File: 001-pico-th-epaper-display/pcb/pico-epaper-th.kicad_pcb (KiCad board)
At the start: 2 copper layers, 70 x 70 mm, 16 parts, among them Q1 AO3407, U1 GY-SHT31-D, U2 TPL5110, U3 WS_1_54_epaper_module

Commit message: name change
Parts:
- added C4: 100n, Capacitor_SMD:C_0603_1608Metric_Pad1.08x0.95mm_HandSolder, F.Cu at (149.2, 74.8)
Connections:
- R1 pad 1: Net-(U2-DELAY/M_DRV) -> VCC
- U2 pad 3: Net-(U2-DELAY/M_DRV) -> VCC
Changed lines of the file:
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@@
 		(embedded_fonts no)
 	)
+	(footprint "Capacitor_SMD:C_0603_1608Metric_Pad1.08x0.95mm_HandSolder"
+		(layer "F.Cu")
+		(at 149.175 74.755)
+		(descr "Capacitor SMD 0603 (1608 Metric), square (rectangular) end terminal, IPC-7351 nominal with elongated pad for handsoldering. (Body size source: IPC-SM-782 page 76, https://www.pcb-3d.com/wordpress/wp-content/uploads/ipc-sm-782a_amendment_1_and_2.pdf)")
+		(tags "capacitor handsolder")
+		(property "Reference" "C4"
+			(at 0 -1.43 0)
+			(layer "F.SilkS")
+			(effects
+				(font
+					(size 1 1)
+					(thickness 0.15)
+				)
+			)
+		)
+		(property "Value" "100n"
+			(at 0 1.43 0)
+			(layer "F.Fab")
+			(effects
+				(font
+					(size 1 1)
+					(thickness 0.15)
+				)
+			)
+		)
+		(property "Datasheet" ""
+			(at 0 0 0)
+			(layer "F.Fab")
+			(hide yes)
+			(effects
+				(font
+					(size 1.27 1.27)
+				)
+			)
+		)
+		(property "Description" "Unpolarized capacitor"
+			(at 0 0 0)
+			(layer "F.Fab")
+			(hide yes)
+			(effects
+				(font
+					(size 1.27 1.27)
+				)
+			)
+		)
+		(property "KiLib_Generator" "SMD_2terminal_chip_molded"
+			(at 0 0 0)
+			(layer "F.SilkS")
+			(hide yes)
+			(effects
+				(font
+					(size 1 1)
+					(thickness 0.15)
+				)
+			)
+		)
+		(property ki_fp_filters "C_*")
+		(sheetname "/")
+		(sheetfile "pico-epaper-th.kicad_sch")
+		(units
+			(unit
+				(name "A")
+				(pins "1" "2")
+			)
+		)
+		(attr smd)
+		(duplicate_pad_numbers_are_jumpers no)
+		(fp_line
+			(start -0.146267 -0.51)
+			(end 0.146267 -0.51)
+			(stroke
+				(width 0.12)
+				(type solid)
+			)
+			(layer "F.SilkS")
+		)
+		(fp_line
+			(start -0.146267 0.51)
+			(end 0.146267 0.51)
+			(stroke
+				(width 0.12)
+				(type solid)
+			)
+			(layer "F.SilkS")
+		)
+		(fp_rect
+			(start -1.65 -0.73)
+			(end 1.65 0.73)
+			(stroke
+				(width 0.05)
+				(type solid)
+			)
+			(fill no)
+			(layer "F.CrtYd")
+		)
+		(fp_rect
+			(start -0.8 -0.4)
+			(end 0.8 0.4)
+			(stroke
+				(width 0.1)
+				(type solid)
+			)
+			(fill no)
+			(layer "F.Fab")
+		)
+		(fp_text user "${REFERENCE}"
+			(at 0 0 0)
+			(layer "F.Fab")
+			(effects
+				(font
+					(size 0.4 0.4)
+					(thickness 0.06)
+				)
+			)
+		)
+		(pad "1" smd roundrect
+			(at -0.8625 0)
+			(size 1.075 0.95)
+			(layers "F.Cu" "F.Mask" "F.Paste")
+			(roundrect_rratio 0.25)
+			(net "Net-(A1-VSYS)")
+			(pintype "passive")
+		)
+		(pad "2" smd roundrect
+			(at 0.8625 0)
+			(size 1.075 0.95)
+			(layers "F.Cu" "F.Mask" "F.Paste")
+			(roundrect_rratio 0.25)
+			(net "GND")
+			(pintype "passive")
+		)
+		(embedded_fonts no)
+		(model "${KICAD10_3DMODEL_DIR}/Capacitor_SMD.3dshapes/C_0603_1608Metric.step"
+			(offset
+				(xyz 0 0 0)
+			)
+			(scale
+				(xyz 1 1 1)
+			)
+			(rotate
+				(xyz 0 0 0)
+			)
+		)
+	)
 	(footprint "MountingHole:MountingHole_2.2mm_M2_Pad"
 		(layer "F.Cu")
@@
 			(layers "F.Cu" "F.Mask" "F.Paste")
 			(roundrect_rratio 0.25)
-			(net "Net-(U2-DELAY{slash}M_DRV)")
+			(net "VCC")
 			(pinfunction "DELAY/M_DRV_3")
 			(pintype "input")
@@
 			(layers "F.Cu" "F.Mask" "F.Paste")
 			(roundrect_rratio 0.25)
-			(net "Net-(U2-DELAY{slash}M_DRV)")
+			(net "VCC")
 			(pintype "passive")
 		)
@@
 		(model "${KIPRJMOD}/AABattery Holder.stp"
 			(offset
-				(xyz -48 -60 -10)
+				(xyz -48 -57 -10)
 			)
 			(scale

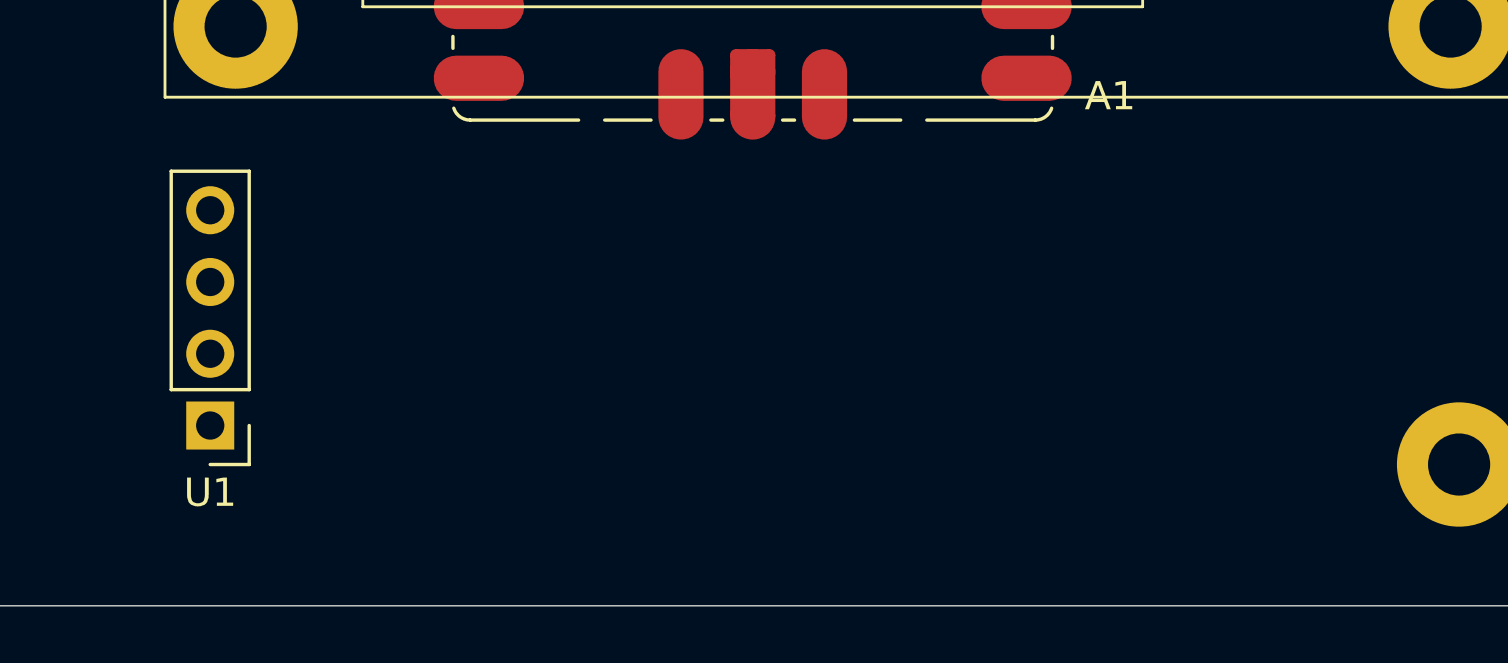
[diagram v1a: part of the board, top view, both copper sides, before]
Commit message: pin changed for sht31
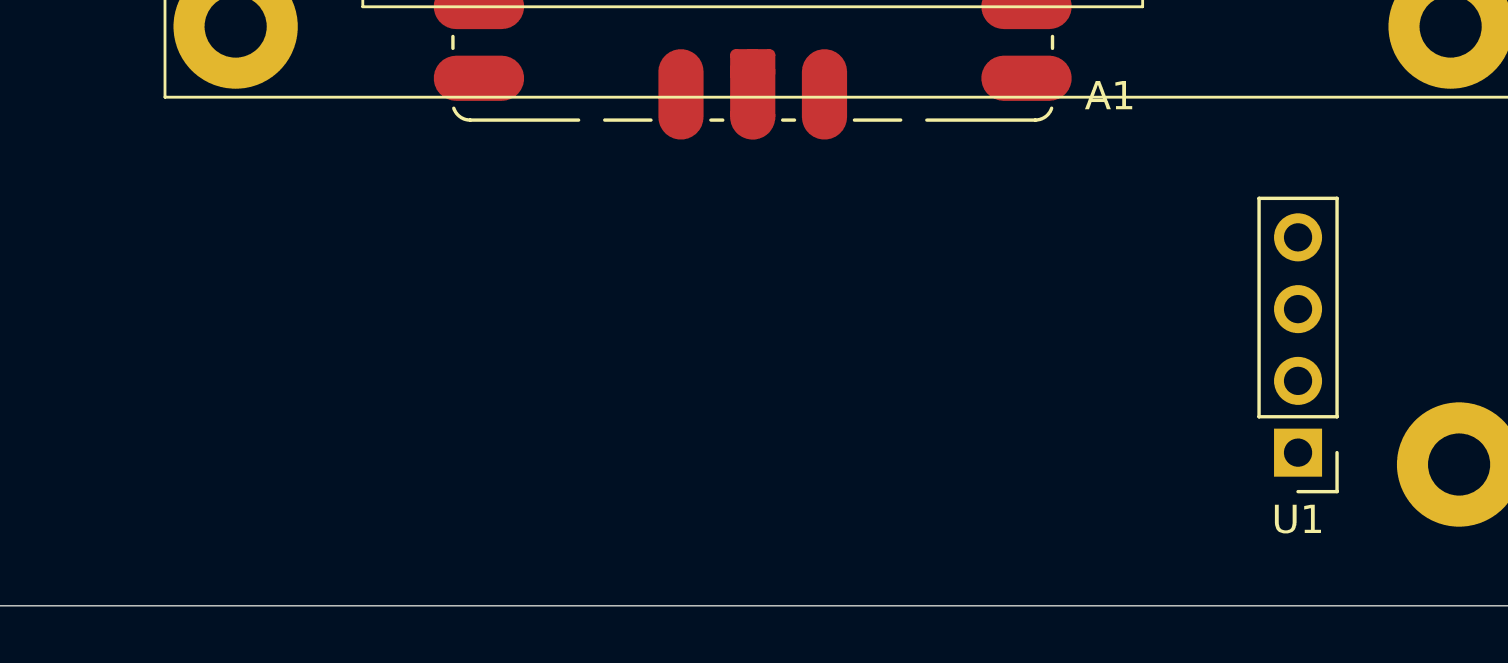
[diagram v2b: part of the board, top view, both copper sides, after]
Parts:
- moved U1 38.5 mm to (154.7, 136.9)
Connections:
- net Net-(A1-3V3) renamed /3V3
- A1 pad 26: unconnected-(A1-GPIO20-Pad26) -> Net-(A1-GPIO20)
- A1 pad 27: unconnected-(A1-GPIO21-Pad27) -> Net-(A1-GPIO21)
- A1 pad 6: Net-(A1-GPIO4) -> unconnected-(A1-GPIO4-Pad6)
- A1 pad 7: Net-(A1-GPIO5) -> unconnected-(A1-GPIO5-Pad7)
- U1 pad 3: Net-(A1-GPIO5) -> Net-(A1-GPIO21)
- U1 pad 4: Net-(A1-GPIO4) -> Net-(A1-GPIO20)
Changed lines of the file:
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@@
 			(layers "*.Cu" "*.Mask")
 			(remove_unused_layers no)
-			(net "Net-(A1-3V3)")
+			(net "/3V3")
 			(pinfunction "VCC_8")
 			(pintype "power_in")
@@
 			(layers "F.Cu" "F.Mask" "F.Paste")
 			(roundrect_rratio 0.25)
-			(net "Net-(A1-3V3)")
+			(net "/3V3")
 			(pintype "passive")
 		)
@@
 	)
 	(footprint "Connector_PinHeader_2.54mm:PinHeader_1x04_P2.54mm_Vertical"
-		(locked yes)
 		(layer "F.Cu")
-		(at 116.2 135.92 180)
+		(at 154.7 136.88 180)
 		(descr "Through hole straight pin header, 1x04, 2.54mm pitch, single row")
 		(tags "Through hole pin header THT 1x04 2.54mm single row")
@@
 			(layers "*.Cu" "*.Mask")
 			(remove_unused_layers no)
-			(net "Net-(A1-3V3)")
+			(net "/3V3")
 			(pinfunction "VCC_1")
 			(pintype "power_in")
@@
 			(layers "*.Cu" "*.Mask")
 			(remove_unused_layers no)
-			(net "Net-(A1-GPIO5)")
+			(net "Net-(A1-GPIO21)")
 			(pinfunction "SCL_3")
 			(pintype "input")
@@
 			(layers "*.Cu" "*.Mask")
 			(remove_unused_layers no)
-			(net "Net-(A1-GPIO4)")
+			(net "Net-(A1-GPIO20)")
 			(pinfunction "SDA_4")
 			(pintype "bidirectional")
@@
 			(layers "F.Cu" "F.Mask")
 			(roundrect_rratio 0.5)
-			(net "Net-(A1-GPIO4)")
+			(net "unconnected-(A1-GPIO4-Pad6)")
 			(pinfunction "GPIO4_6")
-			(pintype "bidirectional")
+			(pintype "bidirectional+no_connect")
 		)
 		(pad "7" smd roundrect
@@
 			(layers "F.Cu" "F.Mask")
 			(roundrect_rratio 0.5)
-			(net "Net-(A1-GPIO5)")
+			(net "unconnected-(A1-GPIO5-Pad7)")
 			(pinfunction "GPIO5_7")
-			(pintype "bidirectional")
+			(pintype "bidirectional+no_connect")
 		)
 		(pad "8" smd custom
@@
 			(layers "F.Cu" "F.Mask")
 			(roundrect_rratio 0.5)
-			(net "unconnected-(A1-GPIO20-Pad26)")
+			(net "Net-(A1-GPIO20)")
 			(pinfunction "GPIO20_26")
-			(pintype "bidirectional+no_connect")
+			(pintype "bidirectional")
 		)
 		(pad "27" smd roundrect
@@
 			(layers "F.Cu" "F.Mask")
 			(roundrect_rratio 0.5)
-			(net "unconnected-(A1-GPIO21-Pad27)")
+			(net "Net-(A1-GPIO21)")
 			(pinfunction "GPIO21_27")
-			(pintype "bidirectional+no_connect")
+			(pintype "bidirectional")
 		)
 		(pad "28" smd custom
@@
 			(layers "F.Cu" "F.Mask")
 			(roundrect_rratio 0.5)
-			(net "Net-(A1-3V3)")
+			(net "/3V3")
 			(pinfunction "3V3_36")
 			(pintype "power_out")

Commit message: pcb routing
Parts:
- moved BT1 19.8 mm to (156.3, 76.0), turned to -90 degrees
- moved R1 14.4 mm to (166.1, 83.5), turned to -90 degrees
- moved C2 7.60 mm to (163.0, 84.5), turned to 0 degrees
- moved Q1 5.49 mm to (155.0, 80.9)
- moved U2 5.45 mm to (163.0, 81.4), turned to 90 degrees
- moved C4 4.44 mm to (150.1, 79.1), turned to -90 degrees
- moved C1 1.36 mm to (148.3, 79.1), turned to -90 degrees
- moved C3 0.28 mm to (149.2, 85.5)
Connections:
- R1 pad 1: VCC -> Net-(U2-DELAY/M_DRV)
- U2 pad 3: VCC -> Net-(U2-DELAY/M_DRV)
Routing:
- net Net-(A1-GPIO8): track 0.00 -> 44.4 mm
- net Net-(A1-GPIO28_ADC2): track 0.00 -> 39.4 mm
- net Net-(A1-GPIO10): track 0.21 -> 37.8 mm
- net Net-(A1-GPIO21): track 0.00 -> 36.6 mm
- net VCC: track 0.00 -> 25.5 mm
- net Net-(A1-GPIO20): track 0.00 -> 25.4 mm
- net Net-(A1-GPIO11): track 0.00 -> 21.7 mm
- net Net-(A1-GPIO9): track 0.00 -> 20.8 mm, vias 0 -> 1
- net Net-(A1-GPIO13): track 0.00 -> 18.8 mm
- net Net-(A1-GPIO12): track 0.00 -> 18.7 mm
- net Net-(Q1-G): track 0.00 -> 14.8 mm, vias 0 -> 2
- net GND: track 0.00 -> 7.52 mm
- net /3V3: track 0.00 -> 3.26 mm
- net Net-(U2-DELAY/M_DRV): track 0.00 -> 2.17 mm
- added copper zone on F.Cu, net GND

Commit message: pcb rounting
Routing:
- net Net-(A1-VSYS): track 0.00 -> 8.36 mm
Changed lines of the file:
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@@
+	)
+	(segment
+		(start 147.9725 77.91)
+		(end 148.3 78.2375)
+		(width 0.8)
+		(layer "F.Cu")
+		(net "Net-(A1-VSYS)")
+	)
+	(segment
+		(start 145.09 77.91)
+		(end 147.9725 77.91)
+		(width 0.8)
+		(layer "F.Cu")
+		(net "Net-(A1-VSYS)")
+	)
+	(segment
+		(start 151.7375 78.2375)
+		(end 153.525 80.025)
+		(width 0.8)
+		(layer "F.Cu")
+		(net "Net-(A1-VSYS)")
+	)
+	(segment
+		(start 153.525 80.025)
+		(end 153.525 80.873089)
+		(width 0.8)
+		(layer "F.Cu")
+		(net "Net-(A1-VSYS)")
+	)
+	(segment
+		(start 150.1 78.2375)
+		(end 151.7375 78.2375)
+		(width 0.8)
+		(layer "F.Cu")
+		(net "Net-(A1-VSYS)")
 	)
 	(segment
